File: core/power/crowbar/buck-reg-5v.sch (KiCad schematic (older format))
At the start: 27 parts, among them P1 CONN_01X02, P2 CONN_01X02, U1 LM25576

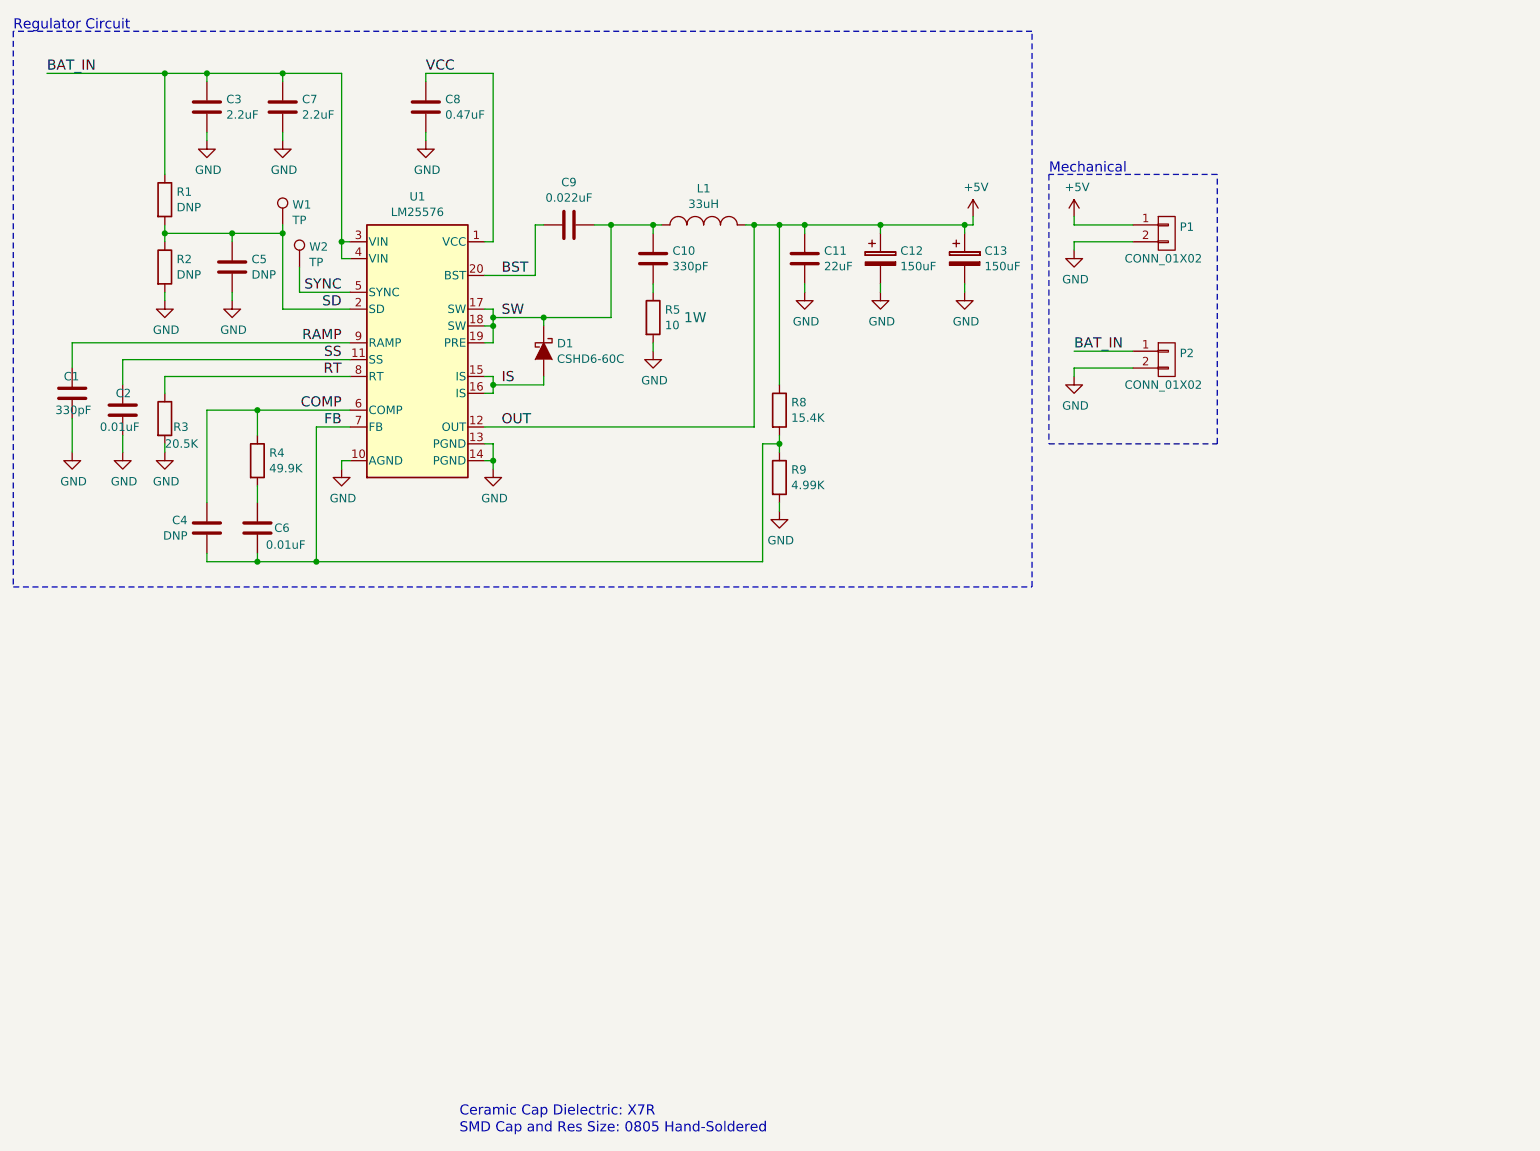
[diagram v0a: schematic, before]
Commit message: Added mfg files. Still needs links to parts.
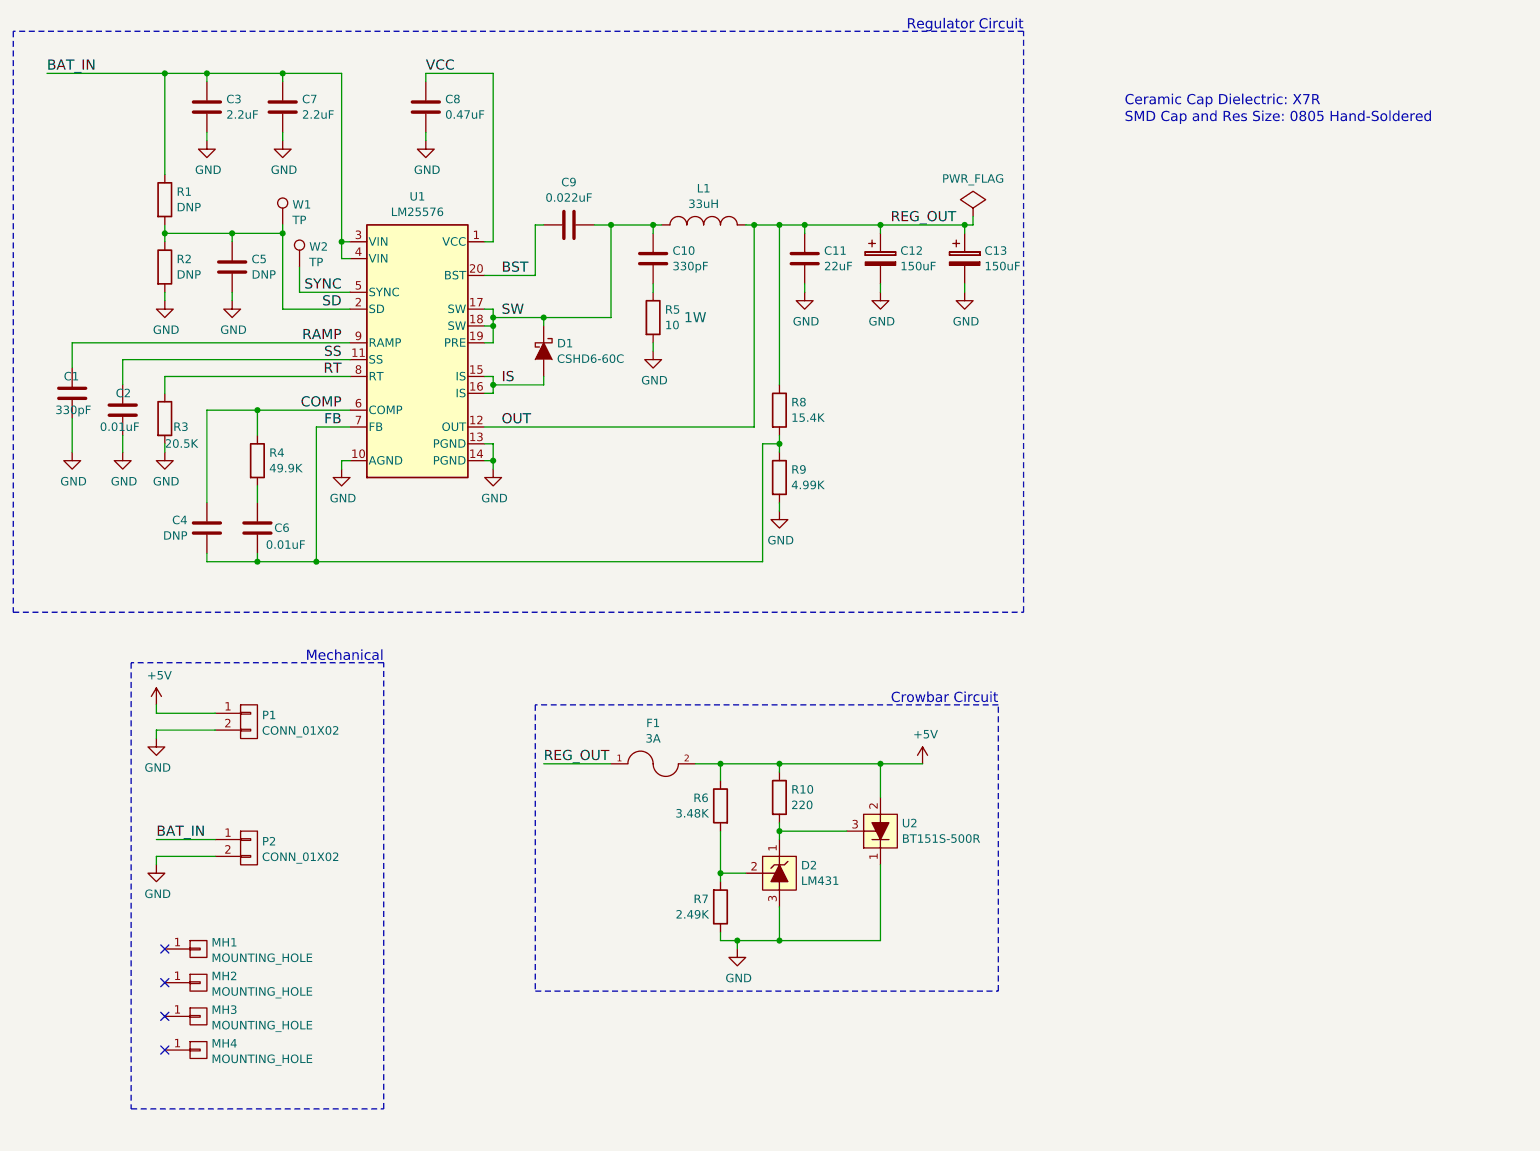
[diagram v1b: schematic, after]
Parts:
- added D2: LM431, TO_SOT_Packages_SMD:SOT-23_Handsoldering, symbol LM431
- added F1: 3A, Resistors_SMD:R_1206_HandSoldering, symbol FUSE
- added MH1, MH2, MH3, MH4: MOUNTING_HOLE, C-BISCUIT:Mounting_Hole_M3x0.5L_~Plate~_~Pad~, symbol CONN_01X01
- added R10: 220, Resistors_SMD:R_0805_HandSoldering, symbol R
- added R6: 3.48K, Resistors_SMD:R_0805_HandSoldering, symbol R
- added R7: 2.49K, Resistors_SMD:R_0805_HandSoldering, symbol R
- added U2: BT151S-500R, TO_SOT_Packages_SMD:TO-252-2Lead, symbol BT151S-500R
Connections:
- net +5V: now also F1.2, R10.1, R6.1, U2.2 (A); no longer C11.1, C12.1, C13.1, L1.2, R8.1, U1.12 (OUT)
- net GND: now also D2.3 (A), R7.1, U2.1 (K)
- new net: D2.1 (K), R10.2, U2.3 (G)
- new net: D2.2 (Ref), R6.2, R7.2
- new net OUT: C11.1, C12.1, C13.1, F1.1, L1.2, R8.1, U1.12 (OUT)
- no-connect marks 0 -> 4
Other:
- note added: "Crowbar Circuit"
- moved on the sheet: P1, P2
